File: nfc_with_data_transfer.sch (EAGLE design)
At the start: 6 parts

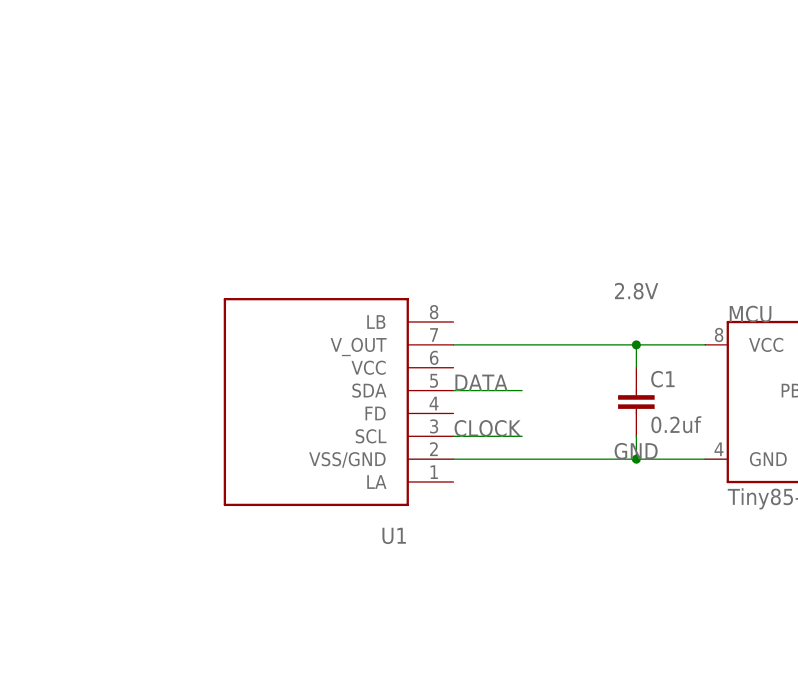
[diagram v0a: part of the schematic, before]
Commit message: Added suggested resistors
Added 4k7 pull-up resistors on SCL and SDA pins. Also added 10 kOhm pull-up resistor on Field Detection line.
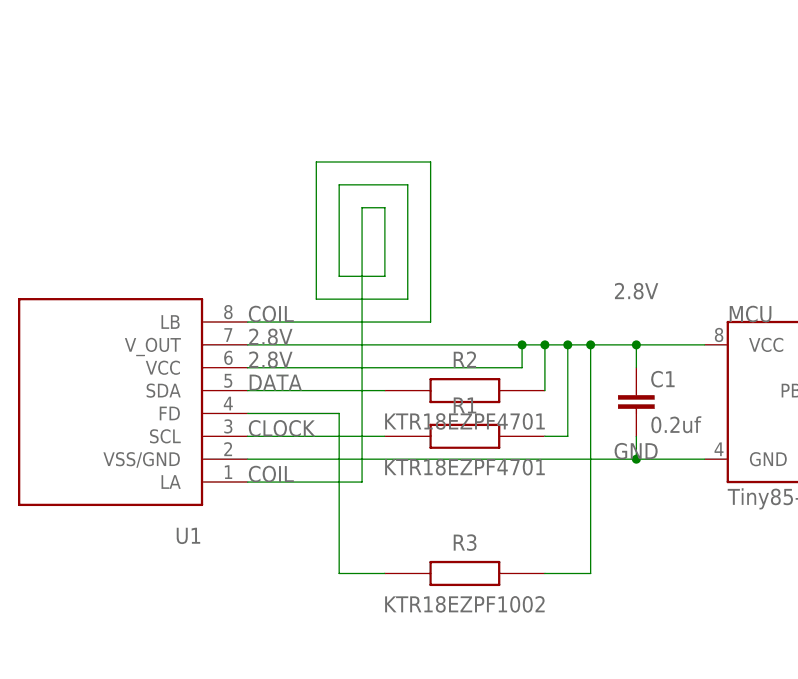
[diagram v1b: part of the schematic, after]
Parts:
- added R1, R2: KTR18EZPF4701, KTR18EZPF4701:KTR18EZPF4701
- added R3: KTR18EZPF1002, KTR18EZPF1002:KTR18EZPF1002
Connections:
- new net COIL: U1.LA, U1.LB
- new net N$2: R3.1, U1.FD
- net 2.8V: now also R1.2, R2.2, R3.2, U1.VCC
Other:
- moved on the sheet: U1
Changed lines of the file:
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@@
 <part name="U1" library="AlterNail" deviceset="NT3H1101" device=""/>
 <part name="C1" library="SparkFun-Capacitors" deviceset="CAP" device="1206" value="0.2uf"/>
+<part name="R1" library="KTR18EZPF4701" deviceset="KTR18EZPF4701" device=""/>
+<part name="R2" library="KTR18EZPF4701" deviceset="KTR18EZPF4701" device=""/>
+<part name="R3" library="KTR18EZPF1002" deviceset="KTR18EZPF1002" device=""/>
 </parts>
 <sheets>
@@
 <instance part="ACCEL" gate="G$1" x="99.06" y="60.96"/>
 <instance part="SJ1" gate="1" x="73.66" y="12.7"/>
-<instance part="U1" gate="G$1" x="0" y="20.32" rot="R180"/>
+<instance part="U1" gate="G$1" x="-22.86" y="20.32" rot="R180"/>
 <instance part="C1" gate="G$1" x="35.56" y="20.32"/>
+<instance part="R1" gate="G$1" x="7.62" y="17.78"/>
+<instance part="R2" gate="G$1" x="7.62" y="22.86"/>
+<instance part="R3" gate="G$1" x="7.62" y="2.54"/>
 </instances>
 <busses>
@@
 <wire x1="43.18" y1="15.24" x2="35.56" y2="15.24" width="0.1524" layer="91"/>
 <pinref part="C1" gate="G$1" pin="2"/>
-<wire x1="35.56" y1="15.24" x2="15.24" y2="15.24" width="0.1524" layer="91"/>
+<wire x1="35.56" y1="15.24" x2="-7.62" y2="15.24" width="0.1524" layer="91"/>
 <wire x1="35.56" y1="17.78" x2="35.56" y2="15.24" width="0.1524" layer="91"/>
 <junction x="35.56" y="15.24"/>
@@
 <label x="33.02" y="33.02" size="1.778" layer="95"/>
 <pinref part="U1" gate="G$1" pin="V_OUT"/>
-<wire x1="35.56" y1="27.94" x2="15.24" y2="27.94" width="0.1524" layer="91"/>
+<wire x1="35.56" y1="27.94" x2="30.48" y2="27.94" width="0.1524" layer="91"/>
 <pinref part="C1" gate="G$1" pin="1"/>
+<wire x1="30.48" y1="27.94" x2="27.94" y2="27.94" width="0.1524" layer="91"/>
+<wire x1="27.94" y1="27.94" x2="25.4" y2="27.94" width="0.1524" layer="91"/>
+<wire x1="25.4" y1="27.94" x2="22.86" y2="27.94" width="0.1524" layer="91"/>
+<wire x1="22.86" y1="27.94" x2="-7.62" y2="27.94" width="0.1524" layer="91"/>
 <wire x1="35.56" y1="25.4" x2="35.56" y2="27.94" width="0.1524" layer="91"/>
 <junction x="35.56" y="27.94"/>
+<pinref part="U1" gate="G$1" pin="VCC"/>
+<wire x1="-7.62" y1="25.4" x2="22.86" y2="25.4" width="0.1524" layer="91"/>
+<wire x1="22.86" y1="25.4" x2="22.86" y2="27.94" width="0.1524" layer="91"/>
+<junction x="22.86" y="27.94"/>
+<pinref part="R2" gate="G$1" pin="2"/>
+<wire x1="25.4" y1="22.86" x2="25.4" y2="27.94" width="0.1524" layer="91"/>
+<pinref part="R1" gate="G$1" pin="2"/>
+<wire x1="25.4" y1="17.78" x2="27.94" y2="17.78" width="0.1524" layer="91"/>
+<wire x1="27.94" y1="17.78" x2="27.94" y2="27.94" width="0.1524" layer="91"/>
+<junction x="25.4" y="27.94"/>
+<junction x="27.94" y="27.94"/>
+<label x="-7.62" y="27.94" size="1.778" layer="95"/>
+<label x="-7.62" y="25.4" size="1.778" layer="95"/>
+<pinref part="R3" gate="G$1" pin="2"/>
+<wire x1="25.4" y1="2.54" x2="30.48" y2="2.54" width="0.1524" layer="91"/>
+<wire x1="30.48" y1="2.54" x2="30.48" y2="27.94" width="0.1524" layer="91"/>
+<junction x="30.48" y="27.94"/>
 </segment>
 </net>
@@
 <segment>
 <pinref part="U1" gate="G$1" pin="SDA"/>
-<wire x1="15.24" y1="22.86" x2="22.86" y2="22.86" width="0.1524" layer="91"/>
-<label x="15.24" y="22.86" size="1.778" layer="95"/>
+<wire x1="-7.62" y1="22.86" x2="7.62" y2="22.86" width="0.1524" layer="91"/>
+<label x="-7.62" y="22.86" size="1.778" layer="95"/>
 </segment>
 <segment>
@@
 <segment>
 <pinref part="U1" gate="G$1" pin="SCL"/>
-<wire x1="15.24" y1="17.78" x2="22.86" y2="17.78" width="0.1524" layer="91"/>
-<label x="15.24" y="17.78" size="1.778" layer="95"/>
+<wire x1="-7.62" y1="17.78" x2="7.62" y2="17.78" width="0.1524" layer="91"/>
+<label x="-7.62" y="17.78" size="1.778" layer="95"/>
 </segment>
 <segment>
@@
 </segment>
 </net>
+<net name="COIL" class="0">
+<segment>
+<pinref part="U1" gate="G$1" pin="LB"/>
+<label x="-7.62" y="30.48" size="1.778" layer="95"/>
+<wire x1="-7.62" y1="30.48" x2="12.7" y2="30.48" width="0.1524" layer="91"/>
+<wire x1="12.7" y1="30.48" x2="12.7" y2="48.26" width="0.1524" layer="91"/>
+<wire x1="12.7" y1="48.26" x2="0" y2="48.26" width="0.1524" layer="91"/>
+<wire x1="0" y1="48.26" x2="0" y2="33.02" width="0.1524" layer="91"/>
+<wire x1="0" y1="33.02" x2="10.16" y2="33.02" width="0.1524" layer="91"/>
+<wire x1="10.16" y1="33.02" x2="10.16" y2="45.72" width="0.1524" layer="91"/>
+<wire x1="10.16" y1="45.72" x2="2.54" y2="45.72" width="0.1524" layer="91"/>
+<wire x1="2.54" y1="45.72" x2="2.54" y2="35.56" width="0.1524" layer="91"/>
+<wire x1="2.54" y1="35.56" x2="7.62" y2="35.56" width="0.1524" layer="91"/>
+<wire x1="7.62" y1="35.56" x2="7.62" y2="43.18" width="0.1524" layer="91"/>
+<wire x1="7.62" y1="43.18" x2="5.08" y2="43.18" width="0.1524" layer="91"/>
+<wire x1="5.08" y1="43.18" x2="5.08" y2="12.7" width="0.1524" layer="91"/>
+<pinref part="U1" gate="G$1" pin="LA"/>
+<label x="-7.62" y="12.7" size="1.778" layer="95"/>
+<wire x1="5.08" y1="12.7" x2="-7.62" y2="12.7" width="0.1524" layer="91"/>
+</segment>
+</net>
+<net name="N$2" class="0">
+<segment>
+<pinref part="U1" gate="G$1" pin="FD"/>
+<wire x1="-7.62" y1="20.32" x2="2.54" y2="20.32" width="0.1524" layer="91"/>
+<wire x1="2.54" y1="20.32" x2="2.54" y2="2.54" width="0.1524" layer="91"/>
+<pinref part="R3" gate="G$1" pin="1"/>
+<wire x1="2.54" y1="2.54" x2="7.62" y2="2.54" width="0.1524" layer="91"/>
+</segment>
+</net>
